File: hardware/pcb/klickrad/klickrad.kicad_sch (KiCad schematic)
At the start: 27 parts, among them J1 SM06B-SRSS-TB, SW1 B3U-1000P, U1 MPR121QR2, U2 DRV2605LDGSR

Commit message: Hauptplatine: Zwischenstand (in Arbeit)
Co-Authored-By: Claude Opus 5.5 <noreply@anthropic.com>
Claude-Session: https://claude.ai/code/session_01JifvE6gExGmwsJWDpfRrrS
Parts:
- removed C6: 10uF, Capacitor_SMD:C_0603_1608Metric, symbol Device:C
- removed SEG1: Touch1, Klickrad:SEG1, symbol Connector:TestPoint
- removed SEG10: Touch10, Klickrad:SEG10, symbol Connector:TestPoint
- removed SEG11: Touch11, Klickrad:SEG11, symbol Connector:TestPoint
- removed SEG12: Touch12, Klickrad:SEG12, symbol Connector:TestPoint
- removed SEG2: Touch2, Klickrad:SEG2, symbol Connector:TestPoint
- removed SEG3: Touch3, Klickrad:SEG3, symbol Connector:TestPoint
- removed SEG4: Touch4, Klickrad:SEG4, symbol Connector:TestPoint
- removed SEG5: Touch5, Klickrad:SEG5, symbol Connector:TestPoint
- removed SEG6: Touch6, Klickrad:SEG6, symbol Connector:TestPoint
- removed SEG7: Touch7, Klickrad:SEG7, symbol Connector:TestPoint
- removed SEG8: Touch8, Klickrad:SEG8, symbol Connector:TestPoint
- removed SEG9: Touch9, Klickrad:SEG9, symbol Connector:TestPoint
- removed SW1: B3U-1000P, Button_Switch_SMD:SW_SPST_B3U-1000P, symbol Switch:SW_Push
- removed U1: MPR121QR2, Klickrad:QFN-20_3x3mm_P0.4mm_noEP, symbol Sensor_Touch:MPR121QR2
- added R10, R4, R5, R6, R7: 10k, Resistor_SMD:R_0402_1005Metric, symbol Device:R
- added R8, R9: 4.7k, Resistor_SMD:R_0402_1005Metric, symbol Device:R
- added SW1: BUTTON, Klickrad:qtouch-button, symbol Connector_Generic:Conn_01x01
- added SW2: WHEEL, Klickrad:qtouch-wheel, symbol Connector_Generic:Conn_01x03
- added SW3: GUARD, Klickrad:qtouch-guard, symbol Connector_Generic:Conn_01x01
- added U1: AT42QT2120, Package_DFN_QFN:VQFN-20-1EP_3x3mm_P0.45mm_EP1.55x1.55mm, symbol Klickrad:AT42QT2120
- C1: Beschreibung MPR121 VDD Entkopplung -> AT42QT2120 VDD, direkt am Pin (Datenblatt 3.4)
- C2: value 0.1uF -> 1uF; Beschreibung MPR121 VREG -> AT42QT2120 VDD Puffer (Tangara C5)
- C3: Beschreibung MPR121 Puffer -> DRV2605L VDD (Tangara C3)
- C4: Beschreibung DRV2605L VDD (1 uF laut Datenblatt) -> DRV2605L REG (Tangara C4)
- C5: value 1uF -> 10uF; footprint Capacitor_SMD:C_0402_1005Metric -> Capacitor_SMD:C_0603_1608Metric; Beschreibung DRV2605L REG (1 uF laut Datenblatt) -> LRA-Stromspitzen (neu gegenueber Tangara)
- J1: Beschreibung JST-SH 6-pol. seitlich -> JST-SH 6-pol. seitlich; Pin 6 = Reserve (BTN)
- R1: value 75k -> 10k; Beschreibung MPR121 REXT 1 % -> Serienwiderstand Wheel-Elektrode 0 (Tangara R1)
- R2: value 4.7k -> 10k; Beschreibung I2C Pull-up SDA, DNP (Hauptboard hat 2,2k) -> Serienwiderstand Wheel-Elektrode 1 (Tangara R2); now fitted
- R3: value 4.7k -> 10k; Beschreibung I2C Pull-up SCL, DNP -> Serienwiderstand Wheel-Elektrode 2 (Tangara R3); now fitted
- TP1: Beschreibung Lötpad LRA Litze + -> Loetpad LRA Litze +
- TP2: Beschreibung Lötpad LRA Litze - -> Loetpad LRA Litze -
- U2: footprint Package_SO:MSOP-10_3x3mm_P0.5mm -> Package_SO:VSSOP-10_3x3mm_P0.5mm; Beschreibung Haptik-Treiber LRA/ERM, I2C 0x5A -> Haptik-Treiber LRA/ERM, I2C 0x5A; IN/TRIG an GND, EN ueber 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
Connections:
- net VREG is gone; now on net 3V3: C2.1
- net 3V3: now also C5.1, R10.1, R6.1, R7.1, R8.1, R9.1, U1.9 (VDD); no longer C4.1, R2.1, R3.1, U2.5 (EN)
- net GND: now also U1.10 (MODE), U1.8 (VSS); no longer R1.2
- net REG: now also C4.1; no longer C5.1
- net SCL: now also R9.2, U1.14 (SCL); no longer R3.2
- net SDA: now also R8.2, U1.11 (SDA); no longer R2.2
- net BTN: no longer names the net of J1.6 (Pin_6)
- net INT renamed CHANGE
- net CHANGE: now also R10.2, U1.15 (~{CHANGE})
- net REXT renamed K0
- net K0: now also U1.7 (KEY0)
- new net E0: R1.2, SW2.1 (Pin_1)
- new net E1: R2.2, SW2.2 (Pin_2)
- new net E2: R3.2, SW2.3 (Pin_3)
- new net EB: R4.2, SW1.1 (Pin_1)
- new net EG: R5.2, SW3.1 (Pin_1)
- new net EN: R7.2, U2.5 (EN)
- new net K1: R2.1, U1.6 (KEY1)
- new net K2: R3.1, U1.5 (KEY2)
- new net KB: R4.1, U1.4 (KEY3)
- new net KG: R5.1, U1.3 (KEY4)
- new net RESET: R6.2, U1.12 (~{RESET})
- no-connect marks 0 -> 8
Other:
- note added: "DRV2605L: VDD 1 uF (+ 10 uF fuer den LRA-Strom), REG 1 uF, EN-Pull-up"
- note added: "I2C-Pull-ups 4,7k: DNP (das Waveshare-Board hat 2,2k). Nur bestuecken, wenn das Modul allein getestet wird."
- note added: "J1 JST-SH 6-pol. (SM06B-SRSS-TB): Pin 6 = BTN (Reserve, nicht beschaltet)"
- note added: "Kupferflaechen vorn (Lackschicht geschlossen): Wheel (3 Elektroden), Mitteltaste, Guard (3 Boegen, ein Netz)"
- note added: "Pins 1, 2, 16-20 (KEY5-KEY11) unbenutzt. CHANGE ist open drain: Pull-up auf der MCU-Seite (R10 nur fuer den Einzeltest)."
- note added: "Serienwiderstaende 10k je Elektrode (Datenblatt 3.1: 4,7k ... 20k), nah am Chip"
- note added: "U1 AT42QT2120 (VQFN-20, Comms-Modus): MODE an GND, I2C 0x1C, KEY0-2 = Wheel, KEY3 = Mitteltaste, KEY4 = Guard"
- note added: "U1 Entkopplung (0,1 uF direkt am Pin) / RESET-Pull-up / CHANGE-Pull-up (DNP)"
- note added: "U2 DRV2605L (VSSOP-10): I2C 0x5A, LRA-Modus, IN/TRIG an GND, EN ueber 10k an 3V3 (wie Tangara)"
- note added: "Wie Tangara: kein Cs noetig (QT2120-Datenblatt: no external Cs required), RESET ueber 10k an 3V3, Exposed Pad ohne Anschluss"
- note removed: "DRV2605L (MSOP-10): I2C 0x5A, LRA-Modus, EN fest an 3V3, IN/TRIG an GND"
- note removed: "DRV2605L Entkopplung (VDD 1uF + 10uF, REG 1uF)"
- note removed: "I2C-Pull-ups 4,7k: DNP (Hauptboard hat 2,2k). Nur bestuecken, wenn Modul allein getestet wird."
- note removed: "J1 JST-SH 6-pol. (SM06B-SRSS-TB)"
- note removed: "MPR121 (QFN-20): ADDR an VDD = I2C 0x5B, REXT 75k, VREG 0,1uF"
- note removed: "MPR121 Entkopplung / REXT / VREG"
- note removed: "Mitteltaste (aktiv low, Pull-up auf MCU-Seite)"
- note removed: "S1 15deg"
- note removed: "S10 285deg"
- note removed: "S11 315deg"
- note removed: "S12 345deg"
- note removed: "S2 45deg"
- note removed: "S3 75deg"
- note removed: "S4 105deg"
- note removed: "S5 135deg"
- note removed: "S6 165deg"
- note removed: "S7 195deg"
- note removed: "S8 225deg"
- note removed: "S9 255deg"
- note removed: "Touch-Segmente (Kupfer vorn, Mitte Winkel 0 = rechts, gegen den Uhrzeigersinn)"
- title: Klickrad-Modul v1 -> Klickrad-Modul v2

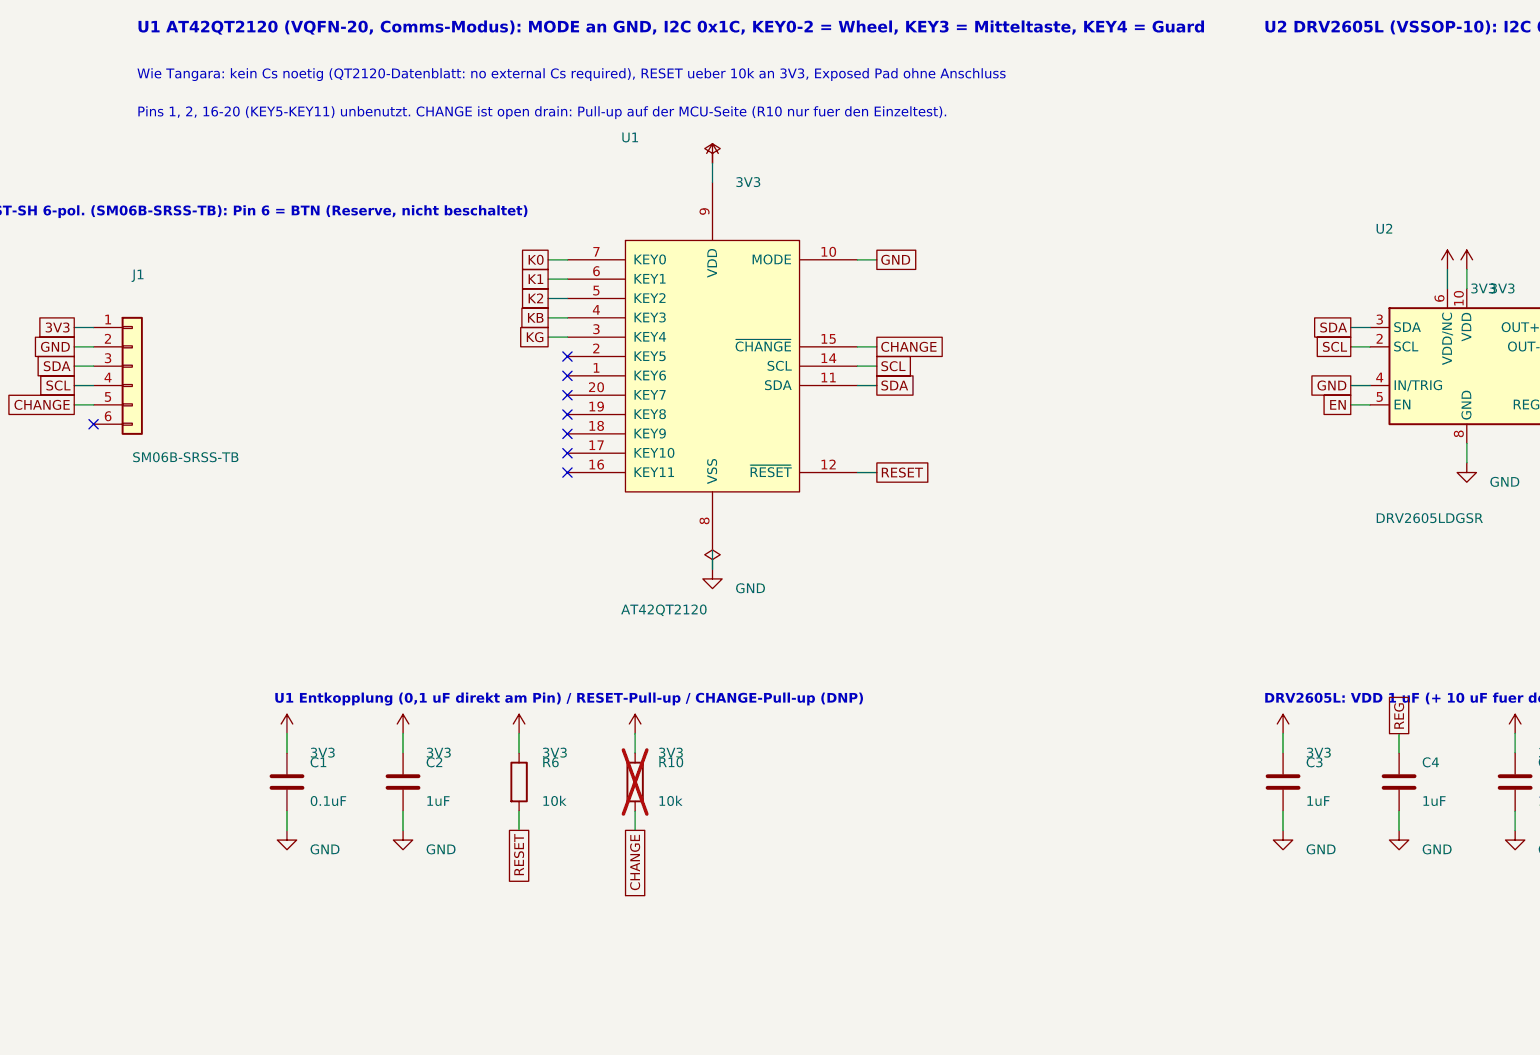
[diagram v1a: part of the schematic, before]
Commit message: Zwischenstand vor Pause: Klickrad v2 und Hauptplatine (unvollständig)
Beide Pakete wurden auf Wunsch angehalten. Klickrad v1 (MPR121) ist der
letzte fertige Stand der Klickrad-Platine in der Historie.

Co-Authored-By: Claude Opus 5.5 <noreply@anthropic.com>
Claude-Session: https://claude.ai/code/session_01JifvE6gExGmwsJWDpfRrrS
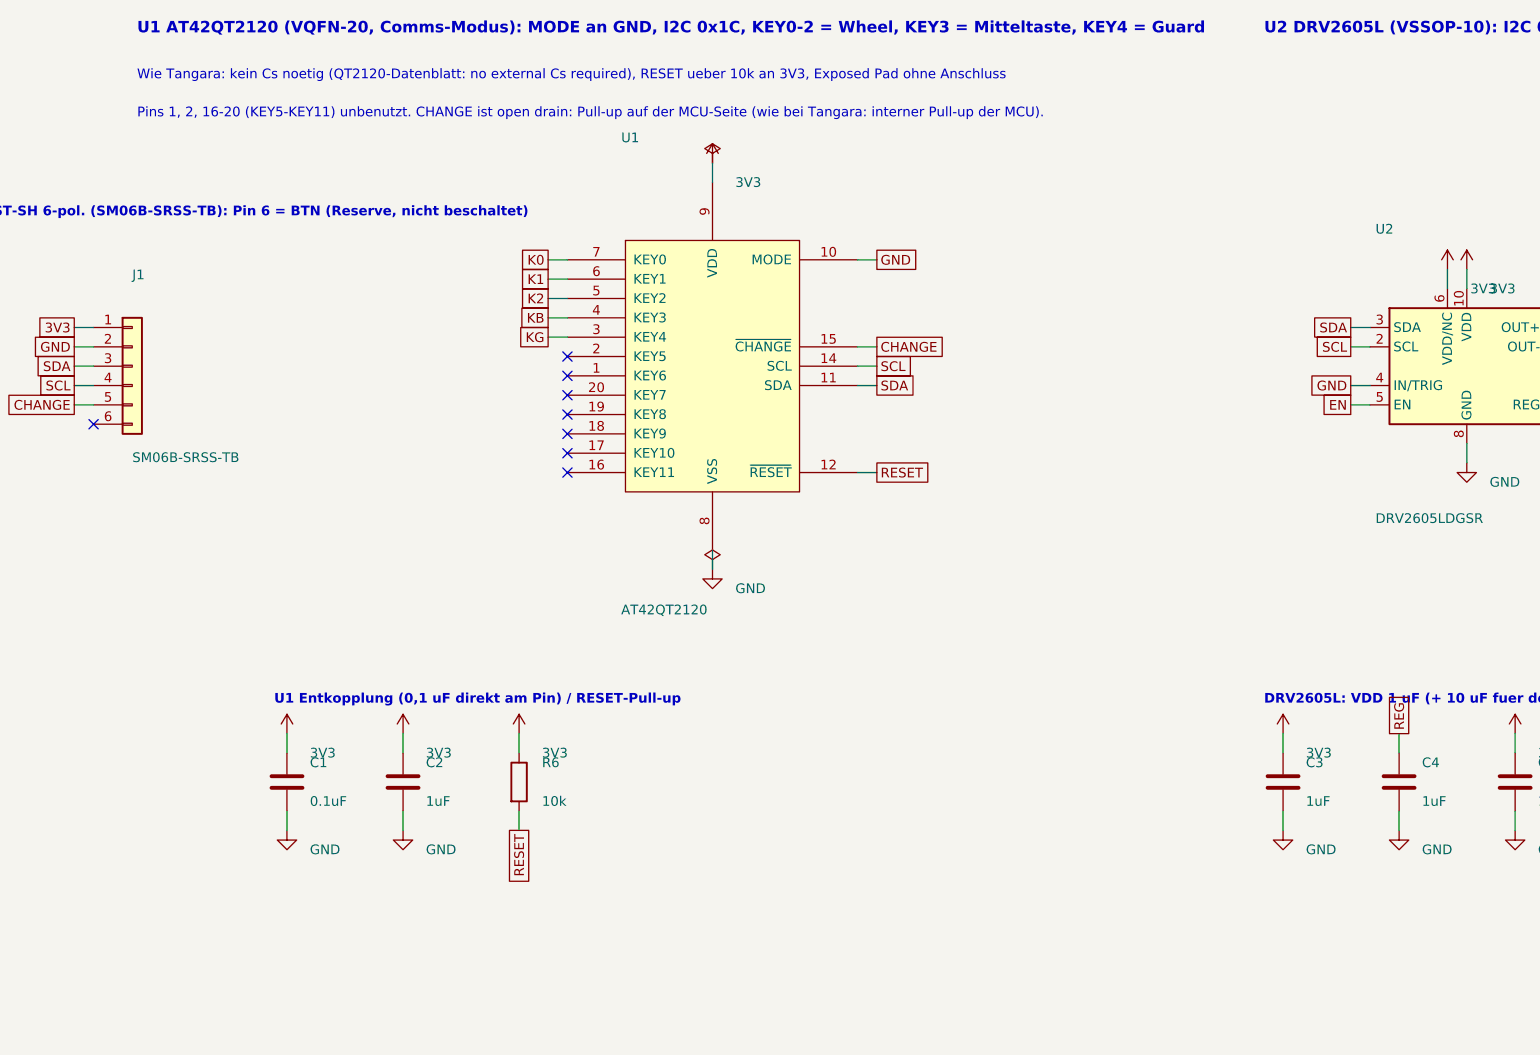
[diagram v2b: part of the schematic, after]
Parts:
- removed R10: 10k, Resistor_SMD:R_0402_1005Metric, symbol Device:R
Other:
- note added: "Pins 1, 2, 16-20 (KEY5-KEY11) unbenutzt. CHANGE ist open drain: Pull-up auf der MCU-Seite (wie bei Tangara: interner Pull-up der MCU)."
- note added: "U1 Entkopplung (0,1 uF direkt am Pin) / RESET-Pull-up"
- note removed: "Pins 1, 2, 16-20 (KEY5-KEY11) unbenutzt. CHANGE ist open drain: Pull-up auf der MCU-Seite (R10 nur fuer den Einzeltest)."
- note removed: "U1 Entkopplung (0,1 uF direkt am Pin) / RESET-Pull-up / CHANGE-Pull-up (DNP)"

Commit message: Platinen: Zwischenstand (in Arbeit)
Co-Authored-By: Claude Opus 5.5 <noreply@anthropic.com>
Claude-Session: https://claude.ai/code/session_01JifvE6gExGmwsJWDpfRrrS
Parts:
- J1: value SM06B-SRSS-TB -> FH12-6S-0.5SH; footprint Connector_JST:JST_SH_SM06B-SRSS-TB_1x06-1MP_P1.00mm_Horizontal -> Connector_FFC-FPC:Hirose_FH12-6S-0.5SH_1x06-1MP_P0.50mm_Horizontal; Beschreibung JST-SH 6-pol. seitlich; Pin 6 = Reserve (BTN) -> FFC/FPC 6-pol., 0,5 mm, Flip-Lock, Bauhöhe 1,0 mm; Pin 6 = 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; Hersteller JST -> Hirose; MPN SM06B-SRSS-TB(LF)(SN) -> FH12-6S-0.5SH(55)
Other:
- note added: "J1 FFC 6-pol. (SM06B-SRSS-TB): Pin 6 = BTN (Reserve, nicht beschaltet)"
- note removed: "J1 JST-SH 6-pol. (SM06B-SRSS-TB): Pin 6 = BTN (Reserve, nicht beschaltet)"
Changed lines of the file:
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@@
 	(title_block (title "Klickrad-Modul v2") (date "2026-10-04") (rev "2") (company "Nano-Player (Hobbyprojekt)")
 		(comment 1 "AT42QT2120 (0x1C, Wheel) + DRV2605L (0x5A, LRA), Beschaltung nach Tangara-Faceplate (CERN-OHL-S-2.0, cool tech zone)")
-		(comment 2 "Schnittstelle laut TEILE.md, Abschnitt Klickrad-Modul; JST-SH 6-pol., Pin 5 = CHANGE, Pin 6 = Reserve"))
+		(comment 2 "Schnittstelle laut TEILE.md, Abschnitt Klickrad-Modul; FFC 6-pol., Pin 5 = CHANGE, Pin 6 = Reserve"))
 	(symbol (lib_id "Klickrad:AT42QT2120") (at 115.57 105.41 0) (unit 1) (exclude_from_sim no) (in_bom yes) (on_board yes) (dnp no)
 		(property "Reference" "U1" (at 103.57 75.41 0) (effects (font (size 1.27 1.27)) (justify left)))
@@
 	(symbol (lib_id "Connector_Generic:Conn_01x06") (at 39.37 105.41 0) (unit 1) (exclude_from_sim no) (in_bom yes) (on_board yes) (dnp no)
 		(property "Reference" "J1" (at 39.37 93.41 0) (effects (font (size 1.27 1.27)) (justify left)))
-		(property "Value" "SM06B-SRSS-TB" (at 39.37 117.41 0) (effects (font (size 1.27 1.27)) (justify left)))
-		(property "Footprint" "Connector_JST:JST_SH_SM06B-SRSS-TB_1x06-1MP_P1.00mm_Horizontal" (at 42.37 105.41 0) (effects (font (size 1.27 1.27)) (justify left) (hide yes)))
+		(property "Value" "FH12-6S-0.5SH" (at 39.37 117.41 0) (effects (font (size 1.27 1.27)) (justify left)))
+		(property "Footprint" "Connector_FFC-FPC:Hirose_FH12-6S-0.5SH_1x06-1MP_P0.50mm_Horizontal" (at 42.37 105.41 0) (effects (font (size 1.27 1.27)) (justify left) (hide yes)))
 		(property "Datasheet" "" (at 42.37 105.41 0) (effects (font (size 1.27 1.27)) (justify left) (hide yes)))
-		(property "MPN" "SM06B-SRSS-TB(LF)(SN)" (at 42.37 105.41 0) (effects (font (size 1.27 1.27)) (justify left) (hide yes)))
-		(property "Hersteller" "JST" (at 42.37 105.41 0) (effects (font (size 1.27 1.27)) (justify left) (hide yes)))
-		(property "Beschreibung" "JST-SH 6-pol. seitlich; Pin 6 = Reserve (BTN)" (at 42.37 105.41 0) (effects (font (size 1.27 1.27)) (justify left) (hide yes)))
+		(property "MPN" "FH12-6S-0.5SH(55)" (at 42.37 105.41 0) (effects (font (size 1.27 1.27)) (justify left) (hide yes)))
+		(property "Hersteller" "Hirose" (at 42.37 105.41 0) (effects (font (size 1.27 1.27)) (justify left) (hide yes)))
+		(property "Beschreibung" "FFC/FPC 6-pol., 0,5 mm, Flip-Lock, Bauhöhe 1,0 mm; Pin 6 = Reserve (BTN)" (at 42.37 105.41 0) (effects (font (size 1.27 1.27)) (justify left) (hide yes)))
 		(pin "1")
 		(pin "2")
@@
 	)
 	(no_connect (at 34.29 113.03))
-	(text "J1 JST-SH 6-pol. (SM06B-SRSS-TB): Pin 6 = BTN (Reserve, nicht beschaltet)" (exclude_from_sim no) (at 18 86 0) (effects (font (size 1.27 1.27) bold) (justify left bottom)))
+	(text "J1 FFC 6-pol. (SM06B-SRSS-TB): Pin 6 = BTN (Reserve, nicht beschaltet)" (exclude_from_sim no) (at 18 86 0) (effects (font (size 1.27 1.27) bold) (justify left bottom)))
 	(symbol (lib_id "Driver_Haptic:DRV2605LDGS") (at 214.63 105.41 0) (unit 1) (exclude_from_sim no) (in_bom yes) (on_board yes) (dnp no)
 		(property "Reference" "U2" (at 202.63 87.41 0) (effects (font (size 1.27 1.27)) (justify left)))
